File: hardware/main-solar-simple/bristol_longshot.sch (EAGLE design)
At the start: 66 parts, among them U1 SAM_D20E, U2 SI4060, U3 UBLOX_MAX, U4 SST25WF040BT-40I/NP, U5 TG-5006CJ, U6 LTC3105EDDPBF, U7 TPS3123, U8 SN74LVC1G32DCKR, U9 BMP180

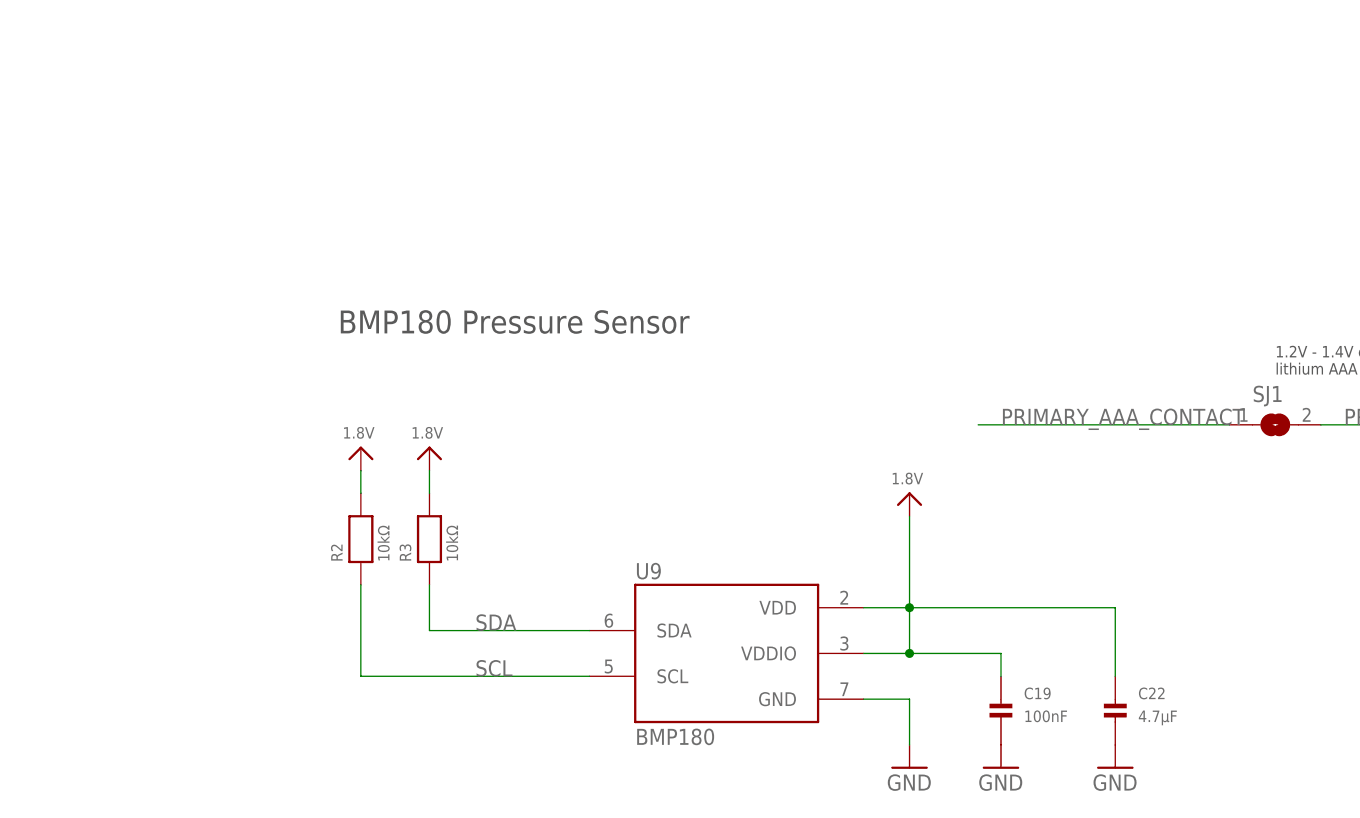
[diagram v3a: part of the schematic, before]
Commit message: Hardware V0.985.2, replaces BMP180 with MS5607
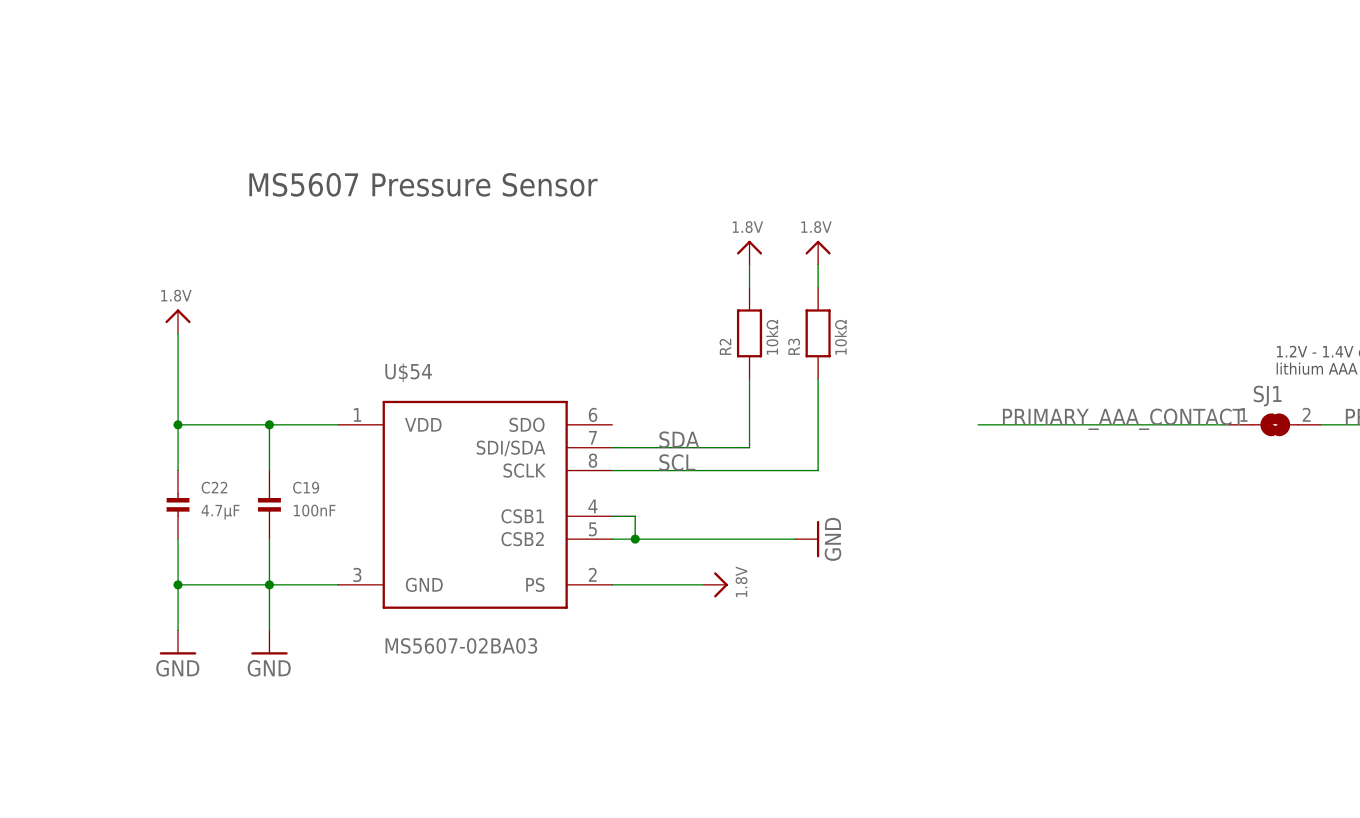
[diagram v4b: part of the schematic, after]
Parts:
- removed U9: BMP180, SparkFun-Sensors:BMP180
- added U$54: MS5607-02BA03, MS5607-02BA03:MS5607-02BA03
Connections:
- net 1.8V: now also U$54.PS, U$54.VDD; no longer U9.VDD, U9.VDDIO
- net GND: now also U$54.CSB1, U$54.CSB2, U$54.GND; no longer U9.GND
- net SCL: now also R3.1, U$54.SCLK; no longer R2.1, U9.SCL
- net SDA: now also R2.1, U$54.SDI/SDA; no longer R3.1, U9.SDA
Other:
- note added: "MS5607 Pressure Sensor"
- note removed: "BMP180 Pressure Sensor"
- moved on the sheet: C19, C22, R2, R3
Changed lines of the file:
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@@
 <part name="JTAG1" library="microbuilder_v3" deviceset="JTAG-CORTEXM3" device="SMT"/>
 <part name="U$4" library="microbuilder_v3" deviceset="1.8V" device=""/>
-<part name="U9" library="SparkFun-Sensors" deviceset="BMP180" device=""/>
-<part name="GND13" library="SparkFun" deviceset="GND" device=""/>
 <part name="C22" library="microbuilder_v3" deviceset="CAP_CERAMIC" device="_0402" value="4.7µF"/>
 <part name="GND20" library="SparkFun" deviceset="GND" device=""/>
@@
 <part name="R13" library="microbuilder_v3" deviceset="RESISTOR" device="_0402" value="56kΩ"/>
 <part name="C19" library="microbuilder_v3" deviceset="CAP_CERAMIC" device="_0402" value="100nF"/>
-<part name="GND1" library="SparkFun" deviceset="GND" device=""/>
 <part name="SJ1" library="microbuilder_v3" deviceset="SOLDERJUMPER" device="REFLOW"/>
 <part name="R7" library="microbuilder_v3" deviceset="RESISTOR" device="_0402" value="0Ω"/>
 <part name="U$52" library="microbuilder_v3" deviceset="GND" device=""/>
 <part name="R8" library="microbuilder_v3" deviceset="RESISTOR" device="_0402" value="DNP"/>
+<part name="U$54" library="MS5607-02BA03" deviceset="MS5607-02BA03" device=""/>
+<part name="GND2" library="SparkFun" deviceset="GND" device=""/>
+<part name="U$55" library="microbuilder_v3" deviceset="1.8V" device=""/>
+<part name="GND1" library="SparkFun" deviceset="GND" device=""/>
 </parts>
 <sheets>
@@
 be disconnected to form a solar midpoint connection</text>
 <text x="30.48" y="-20.32" size="2.54" layer="97" font="vector" ratio="11">LTC3105 Boost Converter</text>
-<text x="38.1" y="-132.08" size="2.54" layer="97" font="vector" ratio="11">BMP180 Pressure Sensor</text>
+<text x="27.94" y="-116.84" size="2.54" layer="97" font="vector" ratio="11">MS5607 Pressure Sensor</text>
 <text x="10.16" y="-12.7" size="6.4516" layer="97" font="vector" ratio="11">Power + Sensor</text>
 <text x="7.62" y="-42.672" size="1.27" layer="97" font="vector" ratio="11">Populate R8 with
@@
 <instance part="JTAG1" gate="G$1" x="25.4" y="157.48"/>
 <instance part="U$4" gate="G$1" x="12.7" y="180.34" rot="MR0"/>
-<instance part="U9" gate="G$1" x="81.28" y="-167.64"/>
-<instance part="GND13" gate="1" x="101.6" y="-180.34"/>
-<instance part="C22" gate="G$1" x="124.46" y="-175.26"/>
-<instance part="GND20" gate="1" x="124.46" y="-180.34"/>
-<instance part="R3" gate="G$1" x="48.26" y="-154.94" rot="R90"/>
-<instance part="R2" gate="G$1" x="40.64" y="-154.94" rot="R90"/>
-<instance part="U$6" gate="G$1" x="40.64" y="-144.78" rot="MR0"/>
-<instance part="U$23" gate="G$1" x="48.26" y="-144.78" rot="MR0"/>
-<instance part="U$35" gate="G$1" x="101.6" y="-149.86" rot="MR0"/>
+<instance part="C22" gate="G$1" x="20.32" y="-152.4"/>
+<instance part="GND20" gate="1" x="20.32" y="-167.64"/>
+<instance part="R3" gate="G$1" x="91.44" y="-132.08" rot="R90"/>
+<instance part="R2" gate="G$1" x="83.82" y="-132.08" rot="R90"/>
+<instance part="U$6" gate="G$1" x="83.82" y="-121.92" rot="MR0"/>
+<instance part="U$23" gate="G$1" x="91.44" y="-121.92" rot="MR0"/>
+<instance part="U$35" gate="G$1" x="81.28" y="-160.02" rot="MR90"/>
 <instance part="D3" gate="A" x="185.42" y="-121.92"/>
 <instance part="D2" gate="A" x="185.42" y="-114.3"/>
@@
 <instance part="U$46" gate="G$1" x="124.46" y="-66.04"/>
 <instance part="R13" gate="G$1" x="124.46" y="-45.72" rot="R90"/>
-<instance part="C19" gate="G$1" x="111.76" y="-175.26"/>
-<instance part="GND1" gate="1" x="111.76" y="-180.34"/>
+<instance part="C19" gate="G$1" x="30.48" y="-152.4"/>
 <instance part="SJ1" gate="1" x="142.24" y="-142.24"/>
 <instance part="R7" gate="G$1" x="185.42" y="-88.9"/>
 <instance part="U$52" gate="G$1" x="175.26" y="-88.9" rot="R270"/>
 <instance part="R8" gate="G$1" x="40.64" y="-40.64"/>
+<instance part="U$54" gate="A" x="53.34" y="-149.86"/>
+<instance part="GND2" gate="1" x="30.48" y="-167.64"/>
+<instance part="U$55" gate="G$1" x="20.32" y="-129.54" rot="MR0"/>
+<instance part="GND1" gate="1" x="91.44" y="-154.94" rot="R90"/>
 </instances>
 <busses>
@@
 </segment>
 <segment>
-<pinref part="U9" gate="G$1" pin="GND"/>
-<pinref part="GND13" gate="1" pin="GND"/>
-<wire x1="96.52" y1="-172.72" x2="101.6" y2="-172.72" width="0.1524" layer="91"/>
-<wire x1="101.6" y1="-172.72" x2="101.6" y2="-177.8" width="0.1524" layer="91"/>
-</segment>
-<segment>
-<pinref part="C22" gate="G$1" pin="P$2"/>
-<pinref part="GND20" gate="1" pin="GND"/>
-</segment>
-<segment>
 <pinref part="R10" gate="G$1" pin="1"/>
 <pinref part="U$48" gate="G$1" pin="GND"/>
@@
 </segment>
 <segment>
-<pinref part="C19" gate="G$1" pin="P$2"/>
-<pinref part="GND1" gate="1" pin="GND"/>
-</segment>
-<segment>
 <pinref part="U$52" gate="G$1" pin="GND"/>
 <pinref part="R7" gate="G$1" pin="1"/>
 <wire x1="177.8" y1="-88.9" x2="180.34" y2="-88.9" width="0.1524" layer="91"/>
+</segment>
+<segment>
+<pinref part="U$54" gate="A" pin="GND"/>
+<pinref part="GND2" gate="1" pin="GND"/>
+<wire x1="38.1" y1="-160.02" x2="30.48" y2="-160.02" width="0.1524" layer="91"/>
+<wire x1="30.48" y1="-160.02" x2="30.48" y2="-165.1" width="0.1524" layer="91"/>
+<pinref part="C19" gate="G$1" pin="P$2"/>
+<wire x1="30.48" y1="-154.94" x2="30.48" y2="-160.02" width="0.1524" layer="91"/>
+<junction x="30.48" y="-160.02"/>
+<pinref part="C22" gate="G$1" pin="P$2"/>
+<pinref part="GND20" gate="1" pin="GND"/>
+<wire x1="20.32" y1="-154.94" x2="20.32" y2="-160.02" width="0.1524" layer="91"/>
+<wire x1="20.32" y1="-160.02" x2="20.32" y2="-165.1" width="0.1524" layer="91"/>
+<wire x1="30.48" y1="-160.02" x2="20.32" y2="-160.02" width="0.1524" layer="91"/>
+<junction x="20.32" y="-160.02"/>
+</segment>
+<segment>
+<pinref part="U$54" gate="A" pin="CSB1"/>
+<wire x1="68.58" y1="-152.4" x2="71.12" y2="-152.4" width="0.1524" layer="91"/>
+<wire x1="71.12" y1="-152.4" x2="71.12" y2="-154.94" width="0.1524" layer="91"/>
+<pinref part="U$54" gate="A" pin="CSB2"/>
+<wire x1="71.12" y1="-154.94" x2="68.58" y2="-154.94" width="0.1524" layer="91"/>
+<wire x1="71.12" y1="-154.94" x2="88.9" y2="-154.94" width="0.1524" layer="91"/>
+<pinref part="GND1" gate="1" pin="GND"/>
+<junction x="71.12" y="-154.94"/>
 </segment>
 </net>
@@
 <segment>
 <pinref part="R2" gate="G$1" pin="2"/>
-<wire x1="40.64" y1="-147.32" x2="40.64" y2="-149.86" width="0.1524" layer="91"/>
+<wire x1="83.82" y1="-124.46" x2="83.82" y2="-127" width="0.1524" layer="91"/>
 <pinref part="U$6" gate="G$1" pin="1.8V"/>
 </segment>
 <segment>
 <pinref part="R3" gate="G$1" pin="2"/>
-<wire x1="48.26" y1="-147.32" x2="48.26" y2="-149.86" width="0.1524" layer="91"/>
+<wire x1="91.44" y1="-124.46" x2="91.44" y2="-127" width="0.1524" layer="91"/>
 <pinref part="U$23" gate="G$1" pin="1.8V"/>
-</segment>
-<segment>
-<pinref part="U9" gate="G$1" pin="VDD"/>
-<wire x1="96.52" y1="-162.56" x2="101.6" y2="-162.56" width="0.1524" layer="91"/>
-<wire x1="101.6" y1="-162.56" x2="101.6" y2="-152.4" width="0.1524" layer="91"/>
-<wire x1="101.6" y1="-167.64" x2="101.6" y2="-162.56" width="0.1524" layer="91"/>
-<junction x="101.6" y="-162.56"/>
-<pinref part="C22" gate="G$1" pin="P$1"/>
-<wire x1="101.6" y1="-162.56" x2="124.46" y2="-162.56" width="0.1524" layer="91"/>
-<wire x1="124.46" y1="-162.56" x2="124.46" y2="-170.18" width="0.1524" layer="91"/>
-<pinref part="U9" gate="G$1" pin="VDDIO"/>
-<wire x1="96.52" y1="-167.64" x2="101.6" y2="-167.64" width="0.1524" layer="91"/>
-<pinref part="U$35" gate="G$1" pin="1.8V"/>
-<pinref part="C19" gate="G$1" pin="P$1"/>
-<wire x1="101.6" y1="-167.64" x2="111.76" y2="-167.64" width="0.1524" layer="91"/>
-<wire x1="111.76" y1="-167.64" x2="111.76" y2="-170.18" width="0.1524" layer="91"/>
-<junction x="101.6" y="-167.64"/>
 </segment>
 <segment>
@@
 <junction x="160.02" y="-38.1"/>
 <junction x="172.72" y="-38.1"/>
+</segment>
+<segment>
+<pinref part="U$54" gate="A" pin="PS"/>
+<pinref part="U$35" gate="G$1" pin="1.8V"/>
+<wire x1="68.58" y1="-160.02" x2="78.74" y2="-160.02" width="0.1524" layer="91"/>
+</segment>
+<segment>
+<pinref part="U$54" gate="A" pin="VDD"/>
+<pinref part="C19" gate="G$1" pin="P$1"/>
+<wire x1="38.1" y1="-142.24" x2="30.48" y2="-142.24" width="0.1524" layer="91"/>
+<wire x1="30.48" y1="-142.24" x2="30.48" y2="-147.32" width="0.1524" layer="91"/>
+<pinref part="U$55" gate="G$1" pin="1.8V"/>
+<wire x1="30.48" y1="-142.24" x2="20.32" y2="-142.24" width="0.1524" layer="91"/>
+<pinref part="C22" gate="G$1" pin="P$1"/>
+<wire x1="20.32" y1="-132.08" x2="20.32" y2="-142.24" width="0.1524" layer="91"/>
+<junction x="20.32" y="-142.24"/>
+<wire x1="20.32" y1="-142.24" x2="20.32" y2="-147.32" width="0.1524" layer="91"/>
+<junction x="30.48" y="-142.24"/>
 </segment>
 </net>
@@
 </segment>
 <segment>
-<pinref part="U9" gate="G$1" pin="SDA"/>
-<wire x1="66.04" y1="-165.1" x2="48.26" y2="-165.1" width="0.1524" layer="91"/>
-<label x="53.34" y="-165.1" size="1.778" layer="95"/>
-<pinref part="R3" gate="G$1" pin="1"/>
-<wire x1="48.26" y1="-165.1" x2="48.26" y2="-160.02" width="0.1524" layer="91"/>
+<pinref part="U$54" gate="A" pin="SDI/SDA"/>
+<pinref part="R2" gate="G$1" pin="1"/>
+<wire x1="68.58" y1="-144.78" x2="83.82" y2="-144.78" width="0.1524" layer="91"/>
+<wire x1="83.82" y1="-144.78" x2="83.82" y2="-137.16" width="0.1524" layer="91"/>
+<label x="73.66" y="-144.78" size="1.778" layer="95"/>
 </segment>
 </net>
@@
 </segment>
 <segment>
-<pinref part="U9" gate="G$1" pin="SCL"/>
-<wire x1="66.04" y1="-170.18" x2="40.64" y2="-170.18" width="0.1524" layer="91"/>
-<label x="53.34" y="-170.18" size="1.778" layer="95"/>
-<pinref part="R2" gate="G$1" pin="1"/>
-<wire x1="40.64" y1="-170.18" x2="40.64" y2="-160.02" width="0.1524" layer="91"/>
-</segment>
-</net>
+<pinref part="U$54" gate="A" pin="SCLK"/>
+<pinref part="R3" gate="G$1" pin="1"/>
+<wire x1="68.58" y1="-147.32" x2="91.44" y2="-147.32" width="0.1524" layer="91"/>
+<wire x1="91.44" y1="-147.32" x2="91.44" y2="-137.16" width="0.1524" layer="91"/>
+<label x="73.66" y="-147.32" size="1.778" layer="95"/>
+</segment>
+</net>

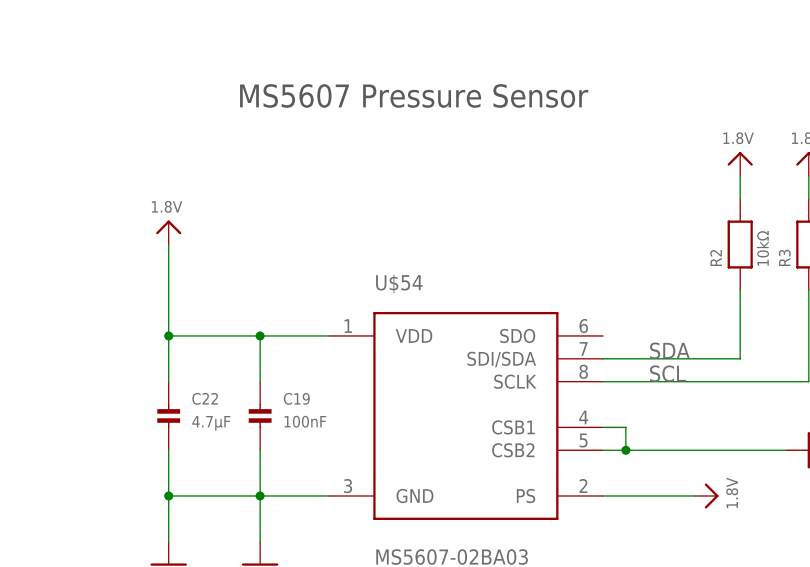
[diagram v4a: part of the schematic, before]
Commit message: Update part name U9
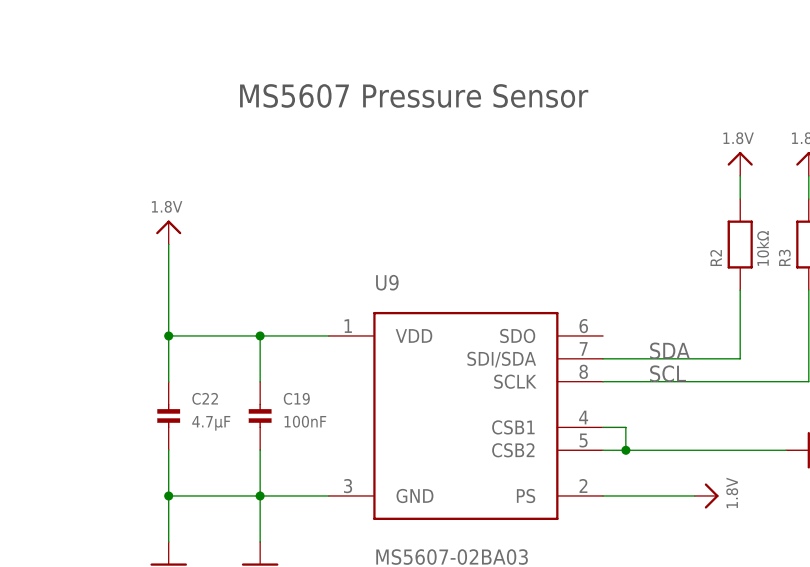
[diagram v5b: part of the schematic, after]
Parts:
- renumbered U$54 to U9
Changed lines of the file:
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@@
 <part name="U$52" library="microbuilder_v3" deviceset="GND" device=""/>
 <part name="R8" library="microbuilder_v3" deviceset="RESISTOR" device="_0402" value="DNP"/>
-<part name="U$54" library="MS5607-02BA03" deviceset="MS5607-02BA03" device=""/>
+<part name="U9" library="MS5607-02BA03" deviceset="MS5607-02BA03" device=""/>
 <part name="GND2" library="SparkFun" deviceset="GND" device=""/>
 <part name="U$55" library="microbuilder_v3" deviceset="1.8V" device=""/>
@@
 <instance part="U$52" gate="G$1" x="175.26" y="-88.9" rot="R270"/>
 <instance part="R8" gate="G$1" x="40.64" y="-40.64"/>
-<instance part="U$54" gate="A" x="53.34" y="-149.86"/>
+<instance part="U9" gate="A" x="53.34" y="-149.86"/>
 <instance part="GND2" gate="1" x="30.48" y="-167.64"/>
 <instance part="U$55" gate="G$1" x="20.32" y="-129.54" rot="MR0"/>
@@
 </segment>
 <segment>
-<pinref part="U$54" gate="A" pin="GND"/>
+<pinref part="U9" gate="A" pin="GND"/>
 <pinref part="GND2" gate="1" pin="GND"/>
 <wire x1="38.1" y1="-160.02" x2="30.48" y2="-160.02" width="0.1524" layer="91"/>
@@
 </segment>
 <segment>
-<pinref part="U$54" gate="A" pin="CSB1"/>
+<pinref part="U9" gate="A" pin="CSB1"/>
 <wire x1="68.58" y1="-152.4" x2="71.12" y2="-152.4" width="0.1524" layer="91"/>
 <wire x1="71.12" y1="-152.4" x2="71.12" y2="-154.94" width="0.1524" layer="91"/>
-<pinref part="U$54" gate="A" pin="CSB2"/>
+<pinref part="U9" gate="A" pin="CSB2"/>
 <wire x1="71.12" y1="-154.94" x2="68.58" y2="-154.94" width="0.1524" layer="91"/>
 <wire x1="71.12" y1="-154.94" x2="88.9" y2="-154.94" width="0.1524" layer="91"/>
@@
 </segment>
 <segment>
-<pinref part="U$54" gate="A" pin="PS"/>
+<pinref part="U9" gate="A" pin="PS"/>
 <pinref part="U$35" gate="G$1" pin="1.8V"/>
 <wire x1="68.58" y1="-160.02" x2="78.74" y2="-160.02" width="0.1524" layer="91"/>
 </segment>
 <segment>
-<pinref part="U$54" gate="A" pin="VDD"/>
+<pinref part="U9" gate="A" pin="VDD"/>
 <pinref part="C19" gate="G$1" pin="P$1"/>
 <wire x1="38.1" y1="-142.24" x2="30.48" y2="-142.24" width="0.1524" layer="91"/>
@@
 </segment>
 <segment>
-<pinref part="U$54" gate="A" pin="SDI/SDA"/>
+<pinref part="U9" gate="A" pin="SDI/SDA"/>
 <pinref part="R2" gate="G$1" pin="1"/>
 <wire x1="68.58" y1="-144.78" x2="83.82" y2="-144.78" width="0.1524" layer="91"/>
@@
 </segment>
 <segment>
-<pinref part="U$54" gate="A" pin="SCLK"/>
+<pinref part="U9" gate="A" pin="SCLK"/>
 <pinref part="R3" gate="G$1" pin="1"/>
 <wire x1="68.58" y1="-147.32" x2="91.44" y2="-147.32" width="0.1524" layer="91"/>

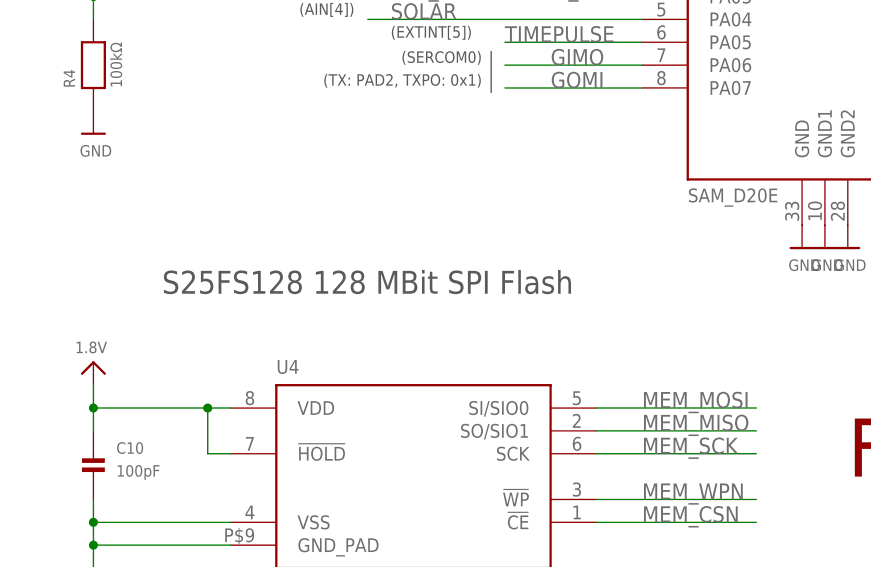
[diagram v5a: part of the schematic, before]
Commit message: main-solar-simple: Fixed mouser part nr for wdt, fixed memory label on schematic
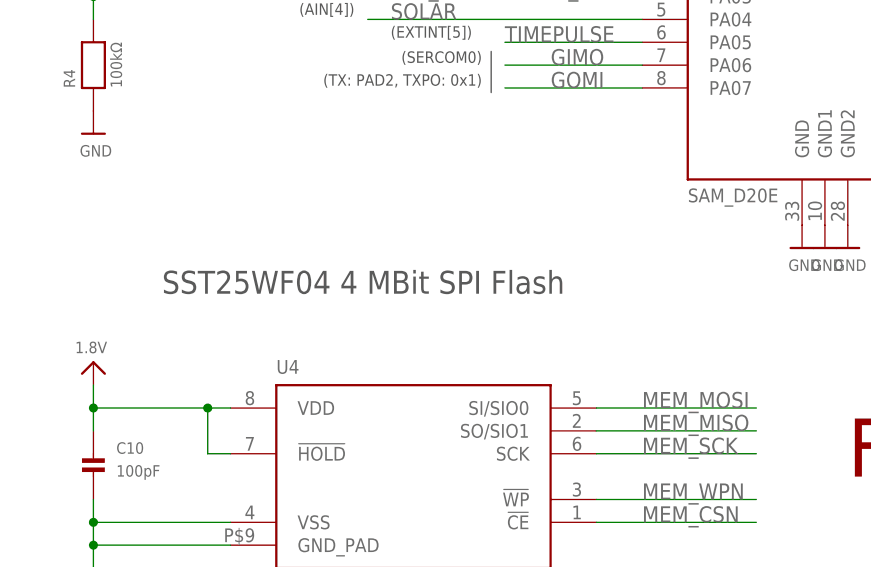
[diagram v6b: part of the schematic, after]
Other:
- note added: "SST25WF04 4 MBit SPI Flash"
- note removed: "S25FS128 128 MBit SPI Flash"
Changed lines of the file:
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@@
 <wire x1="110.236" y1="72.644" x2="110.236" y2="68.072" width="0.1524" layer="97"/>
 <text x="109.22" y="68.834" size="1.27" layer="97" font="vector" ratio="11" rot="MR0">(TX: PAD2, TXPO: 0x1)</text>
-<text x="73.66" y="45.72" size="2.54" layer="97" font="vector" ratio="11">S25FS128 128 MBit SPI Flash</text>
+<text x="73.66" y="45.72" size="2.54" layer="97" font="vector" ratio="11">SST25WF04 4 MBit SPI Flash</text>
 <text x="76.2" y="8.128" size="1.27" layer="97" font="vector" ratio="11" distance="100">Variant is S25FS128SAGNFI101</text>
 <text x="274.32" y="71.12" size="2.54" layer="97" font="vector" ratio="11">MAX8C GPS</text>
